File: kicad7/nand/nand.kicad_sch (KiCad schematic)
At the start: 1 part, among them J1 Conn_01x06_Pin

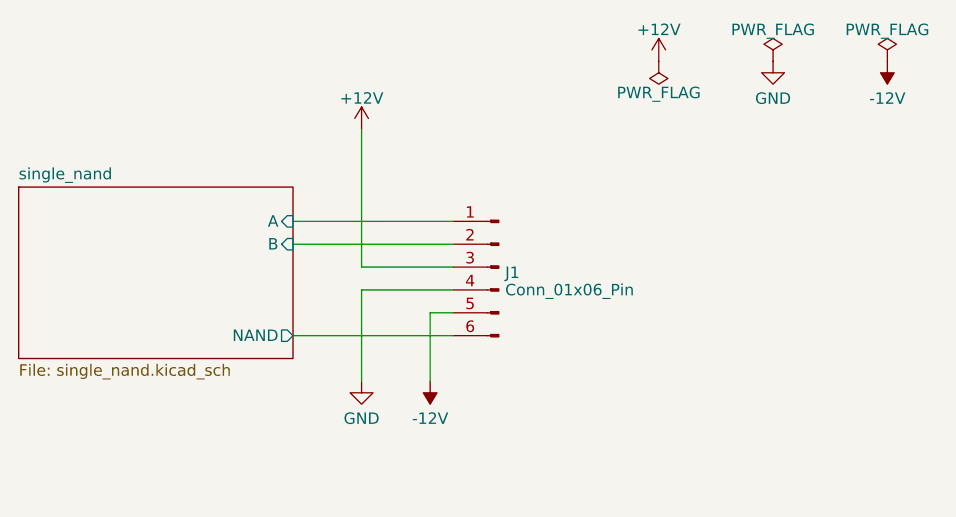
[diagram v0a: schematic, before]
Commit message: alt nand submodule layout. looking better but a lot of jumpers
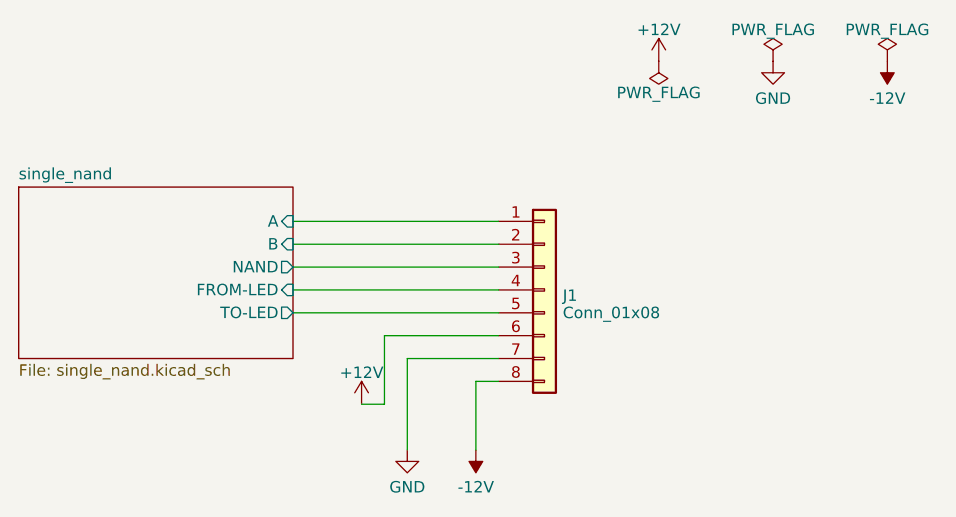
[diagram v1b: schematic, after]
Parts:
- removed J1: Conn_01x06_Pin, Connector_PinHeader_2.54mm:PinHeader_1x06_P2.54mm_Horizontal, symbol Connector:Conn_01x06_Pin
- added J1: Conn_01x08, Connector_PinHeader_2.54mm:PinHeader_1x08_P2.54mm_Horizontal, symbol Connector_Generic:Conn_01x08
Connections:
- net +12V: now also J1.6 (Pin_6)
- net -12V: now also J1.8 (Pin_8)
- net GND: now also J1.7 (Pin_7)
- net single_nand/A: now also J1.1 (Pin_1)
- net single_nand/B: now also J1.2 (Pin_2)
- net single_nand/NAND: now also J1.3 (Pin_3)
- new net single_nand/FROM-LED: J1.4 (Pin_4)
- new net single_nand/TO-LED: J1.5 (Pin_5)
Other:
- sheet single_nand ports: added FROM-LED, TO-LED; removed none
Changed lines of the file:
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@@
 (kicad_sch (version 20230121) (generator eeschema)
   (paper "A4")
-  (wire (pts (xy 76.2 43.18) (xy 93.98 43.18))
-    (stroke (width 0) (type default))
-  )
-  (wire (pts (xy 93.98 50.8) (xy 83.82 50.8))
-    (stroke (width 0) (type default))
-  )
-  (wire (pts (xy 76.2 55.88) (xy 93.98 55.88))
-    (stroke (width 0) (type default))
-  )
-  (wire (pts (xy 93.98 53.34) (xy 91.44 53.34))
-    (stroke (width 0) (type default))
-  )
-  (wire (pts (xy 91.44 53.34) (xy 91.44 60.96))
-    (stroke (width 0) (type default))
-  )
-  (wire (pts (xy 83.82 33.02) (xy 83.82 48.26))
-    (stroke (width 0) (type default))
-  )
-  (wire (pts (xy 83.82 48.26) (xy 93.98 48.26))
-    (stroke (width 0) (type default))
-  )
-  (wire (pts (xy 83.82 50.8) (xy 83.82 60.96))
-    (stroke (width 0) (type default))
-  )
-  (wire (pts (xy 76.2 45.72) (xy 93.98 45.72))
+  (wire (pts (xy 76.2 43.18) (xy 99.06 43.18))
+    (stroke (width 0) (type default))
+  )
+  (wire (pts (xy 76.2 48.26) (xy 99.06 48.26))
+    (stroke (width 0) (type default))
+  )
+  (wire (pts (xy 83.82 63.5) (xy 86.36 63.5))
+    (stroke (width 0) (type default))
+  )
+  (wire (pts (xy 88.9 58.42) (xy 99.06 58.42))
+    (stroke (width 0) (type default))
+  )
+  (wire (pts (xy 76.2 53.34) (xy 99.06 53.34))
+    (stroke (width 0) (type default))
+  )
+  (wire (pts (xy 86.36 63.5) (xy 86.36 55.88))
+    (stroke (width 0) (type default))
+  )
+  (wire (pts (xy 99.06 60.96) (xy 96.52 60.96))
+    (stroke (width 0) (type default))
+  )
+  (wire (pts (xy 86.36 55.88) (xy 99.06 55.88))
+    (stroke (width 0) (type default))
+  )
+  (wire (pts (xy 96.52 60.96) (xy 96.52 68.58))
+    (stroke (width 0) (type default))
+  )
+  (wire (pts (xy 88.9 58.42) (xy 88.9 68.58))
+    (stroke (width 0) (type default))
+  )
+  (wire (pts (xy 76.2 45.72) (xy 99.06 45.72))
+    (stroke (width 0) (type default))
+  )
+  (wire (pts (xy 76.2 50.8) (xy 99.06 50.8))
     (stroke (width 0) (type default))
   )
@@
     )
   )
-  (symbol (lib_id "Connector:Conn_01x06_Pin") (at 99.06 48.26 0) (mirror y) (unit 1)
-    (in_bom yes) (on_board yes) (dnp no) (fields_autoplaced)
-    (property "Reference" "J1" (at 99.7712 48.8863 0)
-      (effects (font (size 1.27 1.27)) (justify right))
-    )
-    (property "Value" "Conn_01x06_Pin" (at 99.7712 50.8073 0)
-      (effects (font (size 1.27 1.27)) (justify right))
-    )
-    (property "Footprint" "Connector_PinHeader_2.54mm:PinHeader_1x06_P2.54mm_Horizontal" (at 99.06 48.26 0)
-      (effects (font (size 1.27 1.27)) hide)
-    )
-    (property "Datasheet" "~" (at 99.06 48.26 0)
+  (symbol (lib_id "power:PWR_FLAG") (at 129.54 25.4 0) (unit 1)
+    (in_bom yes) (on_board yes) (dnp no) (fields_autoplaced)
+    (property "Reference" "#FLG02" (at 129.54 23.495 0)
+      (effects (font (size 1.27 1.27)) hide)
+    )
+    (property "Value" "PWR_FLAG" (at 129.54 21.8981 0)
+      (effects (font (size 1.27 1.27)))
+    )
+    (property "Footprint" "" (at 129.54 25.4 0)
+      (effects (font (size 1.27 1.27)) hide)
+    )
+    (property "Datasheet" "~" (at 129.54 25.4 0)
+      (effects (font (size 1.27 1.27)) hide)
+    )
+    (pin "1")
+    (instances
+      (project "nand"
+        (path "/f93cbd5a-5ca8-4fa6-8951-67f1e1c8b47a"
+          (reference "#FLG02") (unit 1)
+        )
+      )
+    )
+  )
+  (symbol (lib_id "Connector_Generic:Conn_01x08") (at 104.14 50.8 0) (unit 1)
+    (in_bom yes) (on_board yes) (dnp no) (fields_autoplaced)
+    (property "Reference" "J1" (at 106.172 51.4263 0)
+      (effects (font (size 1.27 1.27)) (justify left))
+    )
+    (property "Value" "Conn_01x08" (at 106.172 53.3473 0)
+      (effects (font (size 1.27 1.27)) (justify left))
+    )
+    (property "Footprint" "Connector_PinHeader_2.54mm:PinHeader_1x08_P2.54mm_Horizontal" (at 104.14 50.8 0)
+      (effects (font (size 1.27 1.27)) hide)
+    )
+    (property "Datasheet" "~" (at 104.14 50.8 0)
       (effects (font (size 1.27 1.27)) hide)
     )
@@
     (pin "5")
     (pin "6")
+    (pin "7")
+    (pin "8")
     (instances
       (project "nand"
@@
     )
   )
-  (symbol (lib_id "power:PWR_FLAG") (at 129.54 25.4 0) (unit 1)
-    (in_bom yes) (on_board yes) (dnp no) (fields_autoplaced)
-    (property "Reference" "#FLG02" (at 129.54 23.495 0)
-      (effects (font (size 1.27 1.27)) hide)
-    )
-    (property "Value" "PWR_FLAG" (at 129.54 21.8981 0)
-      (effects (font (size 1.27 1.27)))
-    )
-    (property "Footprint" "" (at 129.54 25.4 0)
-      (effects (font (size 1.27 1.27)) hide)
-    )
-    (property "Datasheet" "~" (at 129.54 25.4 0)
-      (effects (font (size 1.27 1.27)) hide)
-    )
-    (pin "1")
-    (instances
-      (project "nand"
-        (path "/f93cbd5a-5ca8-4fa6-8951-67f1e1c8b47a"
-          (reference "#FLG02") (unit 1)
-        )
-      )
-    )
-  )
-  (symbol (lib_id "power:+12V") (at 83.82 33.02 0) (unit 1)
+  (symbol (lib_id "power:+12V") (at 83.82 63.5 0) (unit 1)
     (in_bom yes) (on_board yes) (dnp no)
-    (property "Reference" "#PWR010" (at 83.82 36.83 0)
-      (effects (font (size 1.27 1.27)) hide)
-    )
-    (property "Value" "+12V" (at 83.82 29.5181 0)
-      (effects (font (size 1.27 1.27)))
-    )
-    (property "Footprint" "" (at 83.82 33.02 0)
-      (effects (font (size 1.27 1.27)) hide)
-    )
-    (property "Datasheet" "" (at 83.82 33.02 0)
+    (property "Reference" "#PWR010" (at 83.82 67.31 0)
+      (effects (font (size 1.27 1.27)) hide)
+    )
+    (property "Value" "+12V" (at 83.82 59.9981 0)
+      (effects (font (size 1.27 1.27)))
+    )
+    (property "Footprint" "" (at 83.82 63.5 0)
+      (effects (font (size 1.27 1.27)) hide)
+    )
+    (property "Datasheet" "" (at 83.82 63.5 0)
       (effects (font (size 1.27 1.27)) hide)
     )
@@
     )
   )
-  (symbol (lib_id "power:GND") (at 83.82 60.96 0) (unit 1)
-    (in_bom yes) (on_board yes) (dnp no) (fields_autoplaced)
-    (property "Reference" "#PWR07" (at 83.82 67.31 0)
-      (effects (font (size 1.27 1.27)) hide)
-    )
-    (property "Value" "GND" (at 83.82 65.0955 0)
-      (effects (font (size 1.27 1.27)))
-    )
-    (property "Footprint" "" (at 83.82 60.96 0)
-      (effects (font (size 1.27 1.27)) hide)
-    )
-    (property "Datasheet" "" (at 83.82 60.96 0)
+  (symbol (lib_id "power:GND") (at 88.9 68.58 0) (unit 1)
+    (in_bom yes) (on_board yes) (dnp no) (fields_autoplaced)
+    (property "Reference" "#PWR07" (at 88.9 74.93 0)
+      (effects (font (size 1.27 1.27)) hide)
+    )
+    (property "Value" "GND" (at 88.9 72.7155 0)
+      (effects (font (size 1.27 1.27)))
+    )
+    (property "Footprint" "" (at 88.9 68.58 0)
+      (effects (font (size 1.27 1.27)) hide)
+    )
+    (property "Datasheet" "" (at 88.9 68.58 0)
       (effects (font (size 1.27 1.27)) hide)
     )
@@
     )
   )
-  (symbol (lib_id "power:-12V") (at 91.44 60.96 0) (mirror x) (unit 1)
-    (in_bom yes) (on_board yes) (dnp no) (fields_autoplaced)
-    (property "Reference" "#PWR08" (at 91.44 63.5 0)
-      (effects (font (size 1.27 1.27)) hide)
-    )
-    (property "Value" "-12V" (at 91.44 65.0955 0)
-      (effects (font (size 1.27 1.27)))
-    )
-    (property "Footprint" "" (at 91.44 60.96 0)
-      (effects (font (size 1.27 1.27)) hide)
-    )
-    (property "Datasheet" "" (at 91.44 60.96 0)
+  (symbol (lib_id "power:-12V") (at 96.52 68.58 0) (mirror x) (unit 1)
+    (in_bom yes) (on_board yes) (dnp no) (fields_autoplaced)
+    (property "Reference" "#PWR08" (at 96.52 71.12 0)
+      (effects (font (size 1.27 1.27)) hide)
+    )
+    (property "Value" "-12V" (at 96.52 72.7155 0)
+      (effects (font (size 1.27 1.27)))
+    )
+    (property "Footprint" "" (at 96.52 68.58 0)
+      (effects (font (size 1.27 1.27)) hide)
+    )
+    (property "Datasheet" "" (at 96.52 68.58 0)
       (effects (font (size 1.27 1.27)) hide)
     )
@@
       (effects (font (size 1.27 1.27)) (justify right))
     )
-    (pin "NAND" output (at 76.2 55.88 0)
-      (effects (font (size 1.27 1.27)) (justify right))
-    )
+    (pin "NAND" output (at 76.2 48.26 0)
+      (effects (font (size 1.27 1.27)) (justify right))
+    )
+    (pin "TO-LED" output (at 76.2 53.34 0)
+      (effects (font (size 1.27 1.27)) (justify right))
+    )
+    (pin "FROM-LED" input (at 76.2 50.8 0)
+      (effects (font (size 1.27 1.27)) (justify right))
+    )
